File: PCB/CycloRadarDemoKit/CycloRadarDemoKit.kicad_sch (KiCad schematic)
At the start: 13 parts, among them J101 I2C conn, J102 Radar pins, J103 CAN, J104 100BASE-T1, J105 Radar debug

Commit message: JLCPCB mistakes repaired, cosmetics on PCB
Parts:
- H101, H102, H103, H104: now left out of the parts list
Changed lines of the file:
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@@
   )
   (symbol (lib_id "Mechanical:MountingHole_Pad") (at 151.765 175.895 270) (unit 1)
-    (in_bom yes) (on_board yes) (dnp no) (fields_autoplaced)
+    (in_bom no) (on_board yes) (dnp no) (fields_autoplaced)
     (property "Reference" "H102" (at 156.21 174.625 90)
       (effects (font (size 1.27 1.27)) (justify left))
@@
   )
   (symbol (lib_id "Mechanical:MountingHole_Pad") (at 151.765 170.18 270) (unit 1)
-    (in_bom yes) (on_board yes) (dnp no) (fields_autoplaced)
+    (in_bom no) (on_board yes) (dnp no) (fields_autoplaced)
     (property "Reference" "H101" (at 156.21 168.91 90)
       (effects (font (size 1.27 1.27)) (justify left))
@@
   )
   (symbol (lib_id "Mechanical:MountingHole_Pad") (at 151.765 181.61 270) (unit 1)
-    (in_bom yes) (on_board yes) (dnp no) (fields_autoplaced)
+    (in_bom no) (on_board yes) (dnp no) (fields_autoplaced)
     (property "Reference" "H103" (at 156.21 180.34 90)
       (effects (font (size 1.27 1.27)) (justify left))
@@
   )
   (symbol (lib_id "Mechanical:MountingHole_Pad") (at 151.765 187.325 270) (unit 1)
-    (in_bom yes) (on_board yes) (dnp no) (fields_autoplaced)
+    (in_bom no) (on_board yes) (dnp no) (fields_autoplaced)
     (property "Reference" "H104" (at 156.21 186.055 90)
       (effects (font (size 1.27 1.27)) (justify left))

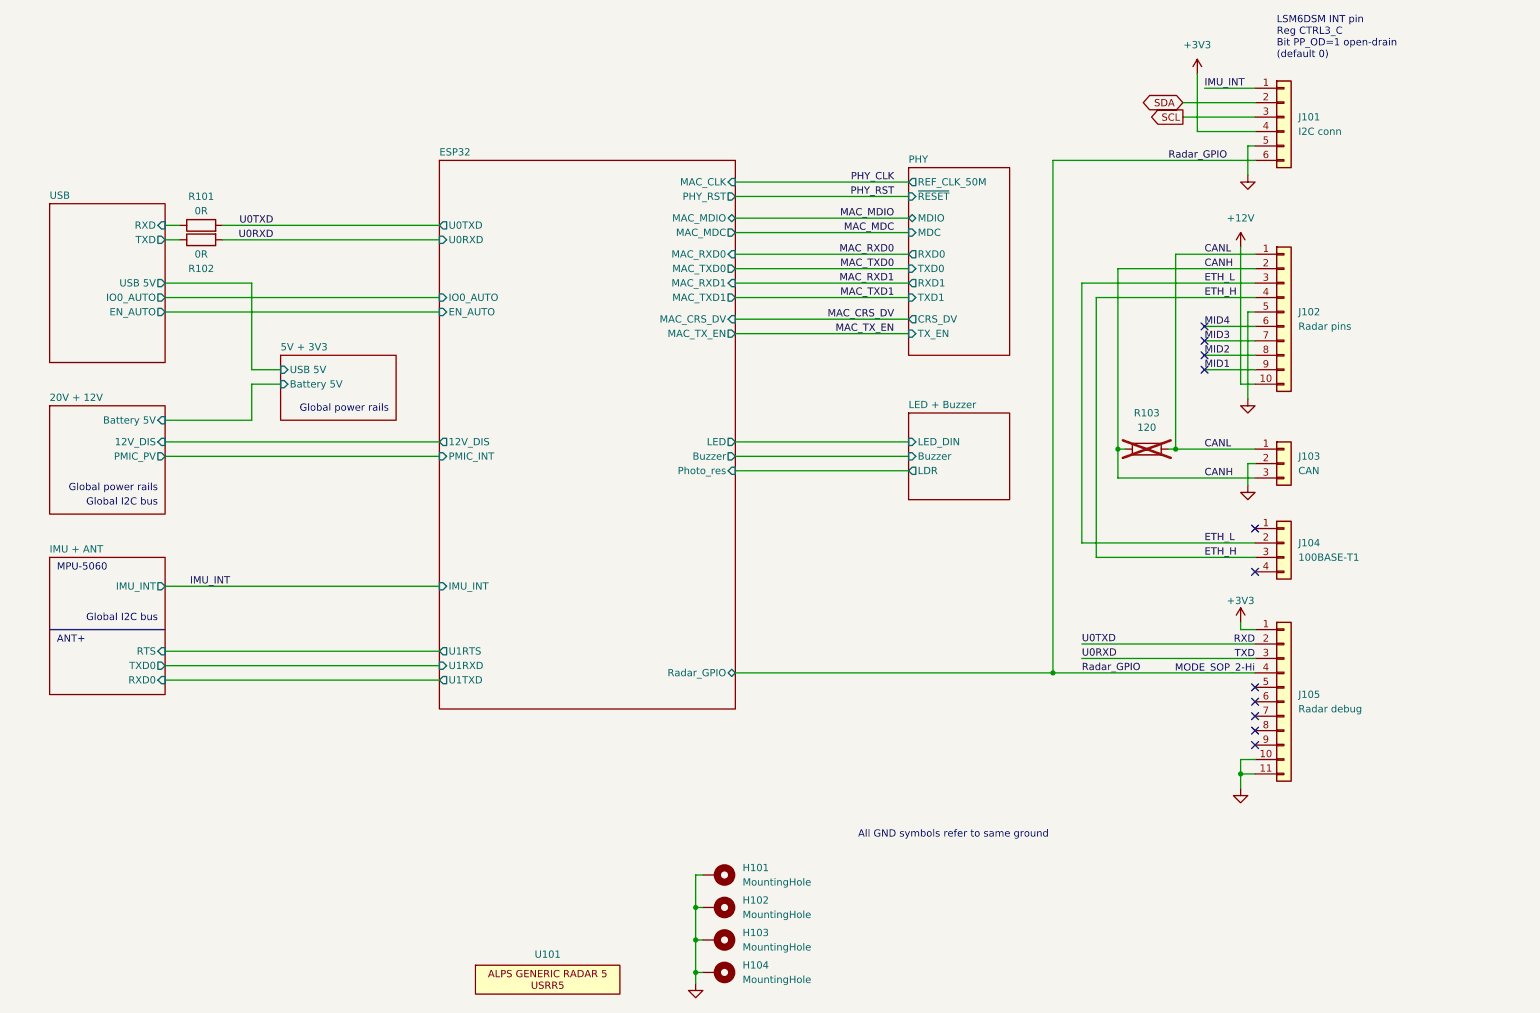
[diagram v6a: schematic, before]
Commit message: Sematic Versioning implemented, whish list added
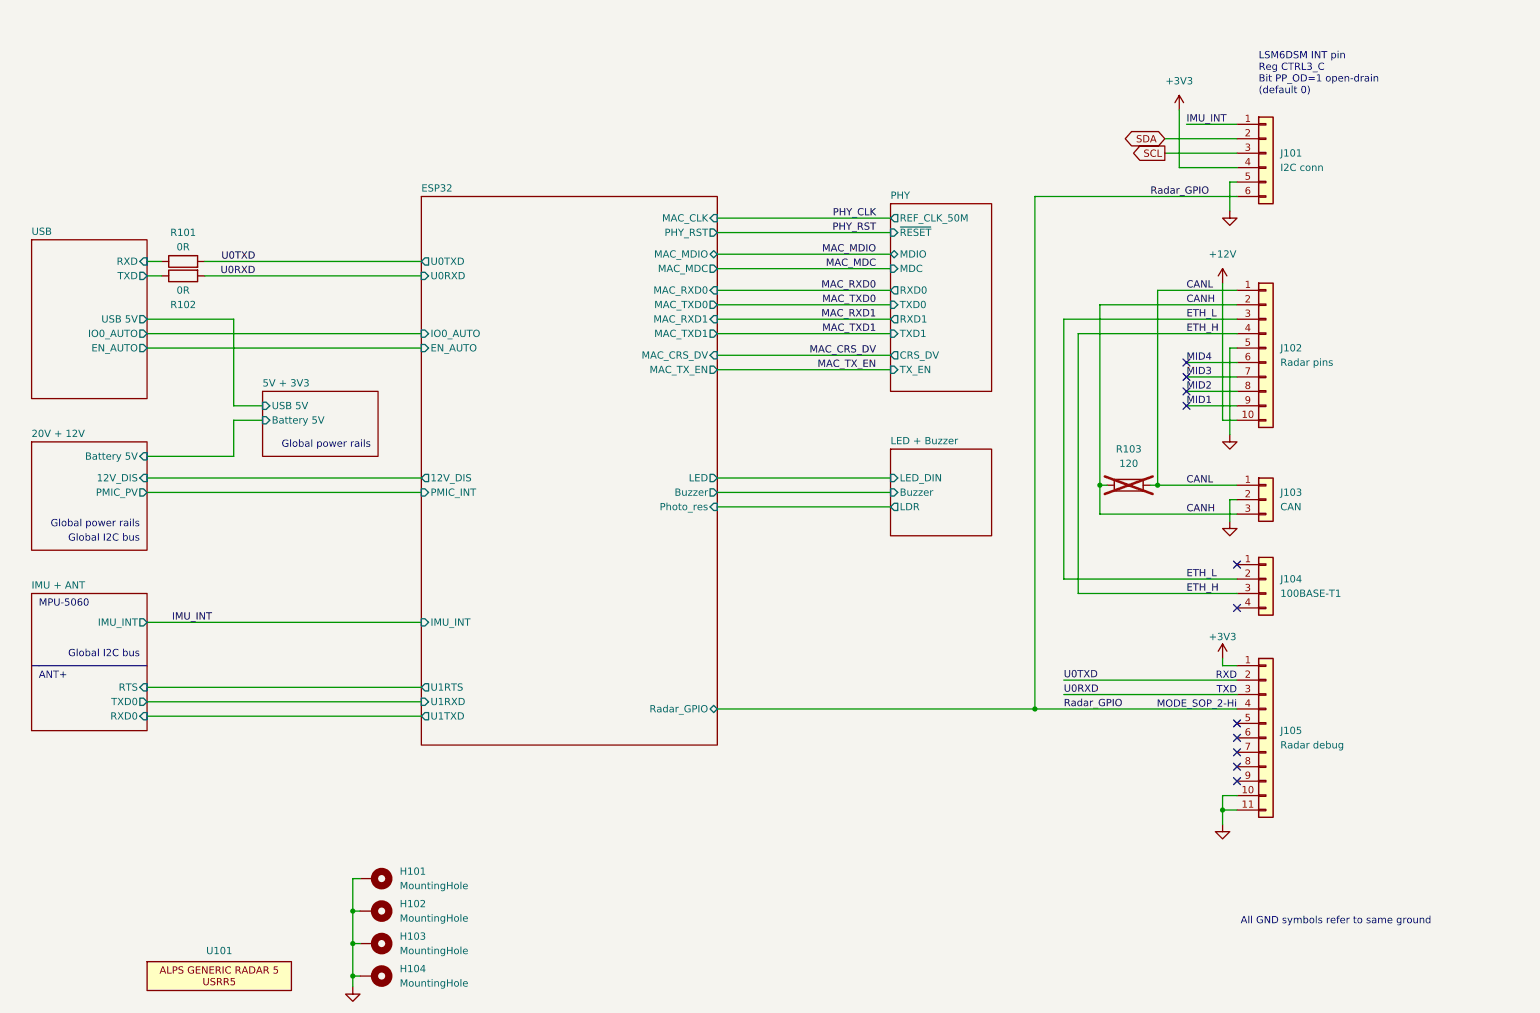
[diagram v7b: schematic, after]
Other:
- company: ALPS Electric Czech, s.r.o. -> ${COMPANY}
- title: Radar Safety Sensor -> ${TITLE}
- moved on the sheet: H101, H102, H103, H104, J101, J102, J103, J104, J105, R101, R102, R103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
